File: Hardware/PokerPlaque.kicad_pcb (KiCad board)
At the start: 2 copper layers, 50 x 43 mm, 7 parts, among them J1 Conn_01x05_Pin, J2 Conn_01x04_Pin, J3 Conn_01x08_Pin, J4 Conn_01x02_Pin, U2 ATtiny1616-M

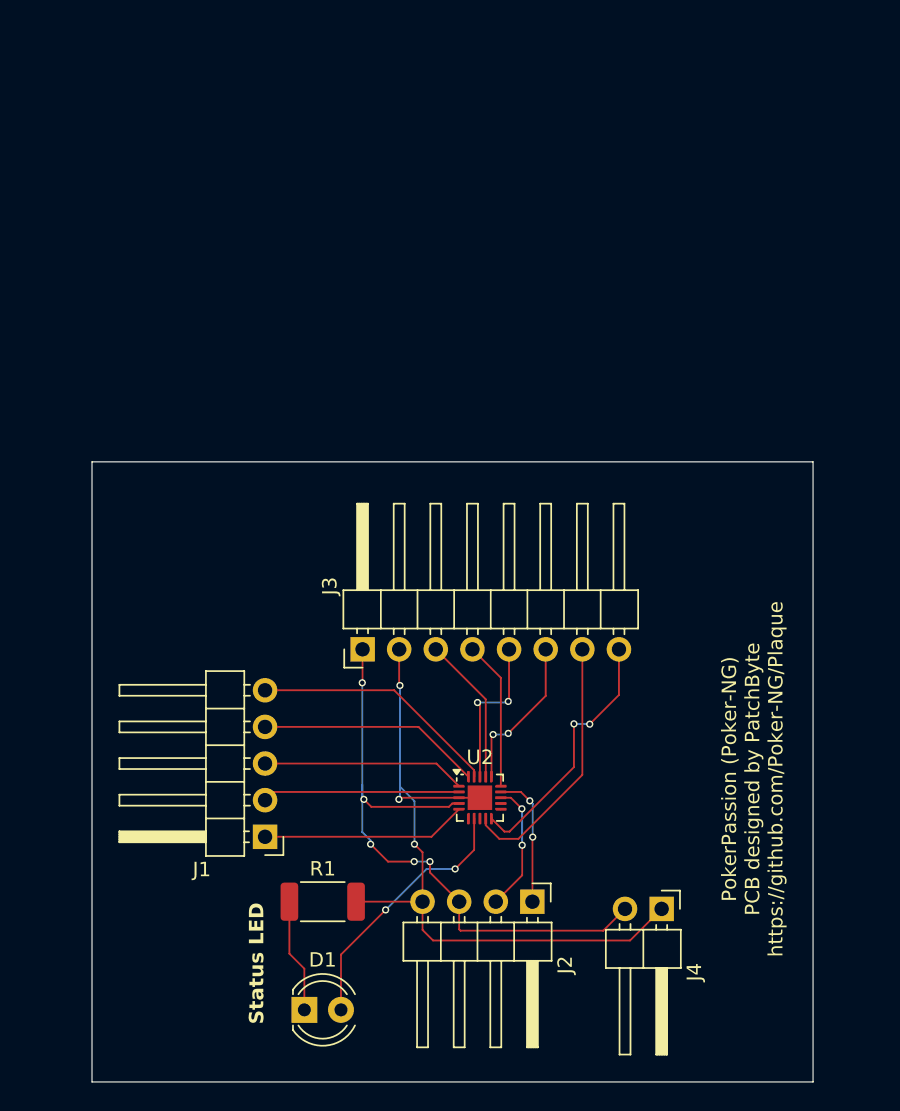
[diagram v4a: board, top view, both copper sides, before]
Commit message: feat: new riscv design
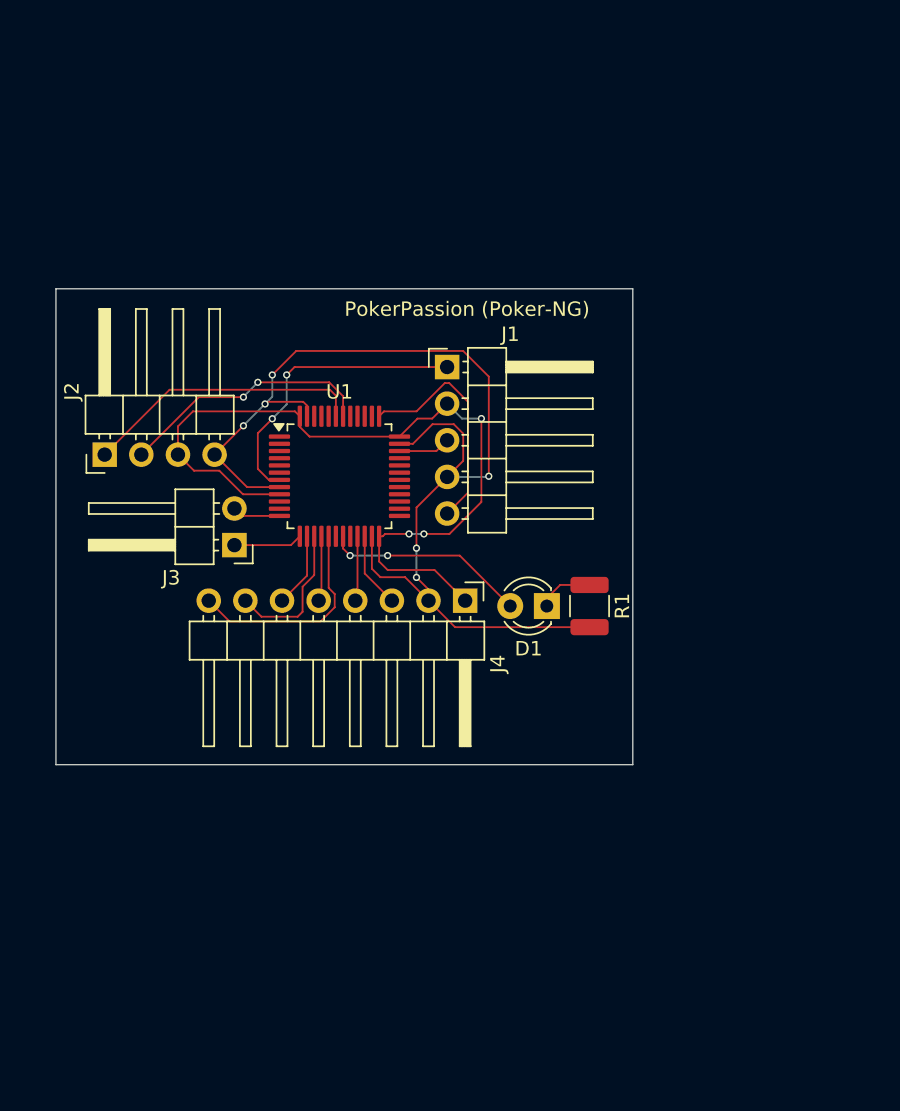
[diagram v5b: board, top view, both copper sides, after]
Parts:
- removed U2: ATtiny1616-M, Package_DFN_QFN:VQFN-20-1EP_3x3mm_P0.4mm_EP1.7x1.7mm
- added U1: CH32V203C8T6, Package_QFP:LQFP-48_7x7mm_P0.5mm, F.Cu at (43.2, 51.0)
- D1: value LED -> NFD3401URD LED; footprint LED_THT:LED_D4.0mm -> LED_THT:LED_D3.0mm
- J3: value Conn_01x08_Pin -> Conn_01x02_Pin; footprint Connector_PinHeader_2.54mm:PinHeader_1x08_P2.54mm_Horizontal -> Connector_PinHeader_2.54mm:PinHeader_1x02_P2.54mm_Horizontal
- J4: value Conn_01x02_Pin -> Conn_01x08_Pin; footprint Connector_PinHeader_2.54mm:PinHeader_1x02_P2.54mm_Horizontal -> Connector_PinHeader_2.54mm:PinHeader_1x08_P2.54mm_Horizontal
- R1: footprint Resistor_SMD:R_2010_5025Metric -> Resistor_SMD:R_1210_3225Metric
- moved J2 42.9 mm to (26.9, 49.5), turned to 90 degrees
- moved J1 34.9 mm to (50.6, 43.4), turned to 0 degrees
- moved D1 32.7 mm to (57.5, 60.0), turned to 180 degrees
- moved R1 27.6 mm to (60.5, 60.0), turned to -90 degrees
- moved J4 25.3 mm to (51.9, 59.6)
- moved J3 11.5 mm to (35.9, 55.8), turned to 180 degrees
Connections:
- D1 pad 2: Led0 -> DEBUG_LED0
- J1 pad 1: /Ss0 -> RST
- J1 pad 2: /Sck0 -> +3.3V
- J1 pad 3: /Miso0 -> SWDIO
- J1 pad 4: /Mosi0 -> GND
- J1 pad 5: /Reset0 -> SWCLK
- J2 pad 1: SCL -> I2C1_SDA
- J2 pad 2: SDA -> I2C1_SCL
- J2 pad 3: VCC -> +3.3V
- J3 pad 1: VCC -> RESERVED_UART_RX
- J3 pad 2: GND -> RESERVED_UART_TX
- J4 pad 1: GND -> +3.3V
- J4 pad 2: VCC -> GND
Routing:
- net +3.3V: track 0.00 -> 56.8 mm, vias 0 -> 3
- net VCC: track 44.0 -> 0.00 mm, vias 5 -> 0
- net GND: track 49.1 -> 80.2 mm, vias 3 -> 6
- net RST: track 0.00 -> 20.5 mm, vias 0 -> 2
- net I2C1_SDA: track 0.00 -> 19.5 mm
- net Led0: track 18.2 -> 0.00 mm, vias 2 -> 0
- net DspRst: track 18.1 -> 0.00 mm
- net DspBusy: track 18.1 -> 0.00 mm, vias 2 -> 0
- net I2C1_SCL: track 0.00 -> 17.9 mm, vias 0 -> 2
- net /Reset0: track 17.3 -> 0.00 mm
- net SWCLK: track 0.00 -> 16.0 mm
- net /Mosi0: track 15.5 -> 0.00 mm
- net DISPLAY_MOSI1: track 0.00 -> 14.8 mm
- net /Ss0: track 14.2 -> 0.00 mm
- net /Miso0: track 14.1 -> 0.00 mm
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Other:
- board size 50 x 43 mm -> 40 x 33 mm
- board text added: "PokerPassion (Poker-NG)"
- board text removed: "PokerPassion (Poker-NG) PCB designed by PatchByte https://github.com/Poker-NG/Plaque"
- board text removed: "Status LED"

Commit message: feat: added some necessities
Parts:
- added R2: 10k Ohm, Resistor_SMD:R_1210_3225Metric, F.Cu at (30.5, 29.5)
- added R3: 10k Ohm, Resistor_SMD:R_1210_3225Metric, F.Cu at (50.5, 57.5)
- added SW1: KH-6X6X6H-STM, Button_Switch_SMD:SW_Push_1P1T_NO_6x6mm_H9.5mm, F.Cu at (51.0, 26.0)
- D1: value NFD3401URD LED -> NFD3401URD
- J1: value Conn_01x05_Pin -> A2541WR-5P
- J2: value Conn_01x04_Pin -> A2541WR-4P
- J3: value Conn_01x02_Pin -> A2541WR-2P
- J4: value Conn_01x08_Pin -> A2541WR-8P
- moved J2 20.0 mm to (34.4, 31.0)
- moved J3 15.7 mm to (24.3, 45.2), turned to 90 degrees
- moved J4 12.2 mm to (45.8, 49.0)
- moved R1 11.9 mm to (50.5, 53.5), turned to 180 degrees
- moved U1 11.6 mm to (36.8, 41.3)
- moved J1 10.5 mm to (44.5, 34.9)
- moved D1 4.64 mm to (54.5, 56.5), turned to 0 degrees
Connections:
- U1 pad 1: unconnected-(U1-VBAT-Pad1) -> +3.3V
- U1 pad 20: unconnected-(U1-PB2-Pad20) -> BOOT1
- U1 pad 44: unconnected-(U1-BOOT0-Pad44) -> BOOT0
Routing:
- net +3.3V: track 56.8 -> 91.5 mm, vias 3 -> 1
- net BOOT0: track 0.00 -> 34.0 mm, vias 0 -> 2
- net BOOT1: track 0.00 -> 24.1 mm
- net DEBUG_LED0: track 14.1 -> 30.2 mm
- net I2C1_SDA: track 19.5 -> 7.05 mm
- net I2C1_SCL: track 17.9 -> 6.21 mm, vias 2 -> 0
- net RESERVED_UART_RX: track 4.79 -> 10.5 mm
- net DISPLAY_MOSI1: track 14.8 -> 10.5 mm, vias 0 -> 2
- net SWCLK: track 16.0 -> 12.2 mm
- net RST: track 20.5 -> 17.5 mm, vias 2 -> 1
- net RESERVED_UART_TX: track 3.34 -> 6.26 mm
- net GND: track 80.2 -> 82.5 mm, vias 6 -> 2
- net DISPLAY_SCK1: track 10.1 -> 8.88 mm
- net DISPLAY_SS1: track 5.18 -> 4.09 mm
- net DISPLAY_MISO1: track 4.54 -> 3.55 mm
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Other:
- board size 40 x 33 mm -> 36.5 x 40.5 mm
- board text removed: "PokerPassion (Poker-NG)"

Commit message: feat: changed some things
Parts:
- moved J3 14.3 mm to (24.2, 30.9)
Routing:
- net RESERVED_UART_RX: track 10.5 -> 21.1 mm, vias 0 -> 2
- net RESERVED_UART_TX: track 6.26 -> 16.2 mm
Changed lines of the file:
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@@
 	(footprint "Connector_PinHeader_2.54mm:PinHeader_1x02_P2.54mm_Horizontal"
 		(layer "F.Cu")
-		(at 24.255248 45.208264 90)
+		(at 24.225 30.875 90)
 		(descr "Through hole angled pin header, 1x02, 2.54mm pitch, 6mm pin length, single row")
 		(tags "Through hole angled pin header THT 1x02 2.54mm single row")
@@
 	)
 	(segment
-		(start 32.5875 44.0875)
-		(end 27.916012 44.0875)
-		(width 0.127)
+		(start 26.765 30.875)
+		(end 28.19 32.3)
+		(width 0.2)
 		(layer "F.Cu")
 		(net 10)
 	)
 	(segment
-		(start 27.916012 44.0875)
-		(end 26.795248 45.208264)
-		(width 0.127)
+		(start 31.5875 44.0875)
+		(end 32.5875 44.0875)
+		(width 0.2)
 		(layer "F.Cu")
 		(net 10)
 	)
 	(segment
-		(start 25.368748 46.321764)
-		(end 33.178236 46.321764)
-		(width 0.127)
+		(start 28.19 32.3)
+		(end 28.19 40.69)
+		(width 0.2)
+		(layer "F.Cu")
+		(net 10)
+	)
+	(segment
+		(start 28.19 40.69)
+		(end 31.5875 44.0875)
+		(width 0.2)
+		(layer "F.Cu")
+		(net 10)
+	)
+	(segment
+		(start 24.225 30.875)
+		(end 24.225 31.925)
+		(width 0.2)
 		(layer "F.Cu")
 		(net 11)
 	)
 	(segment
-		(start 33.178236 46.321764)
+		(start 31.5 45.5)
 		(end 34 45.5)
-		(width 0.127)
+		(width 0.2)
 		(layer "F.Cu")
 		(net 11)
 	)
 	(segment
-		(start 24.255248 45.208264)
-		(end 25.368748 46.321764)
-		(width 0.127)
+		(start 25.8 33.5)
+		(end 27.5 33.5)
+		(width 0.2)
 		(layer "F.Cu")
 		(net 11)
 	)
+	(segment
+		(start 24.225 31.925)
+		(end 25.8 33.5)
+		(width 0.2)
+		(layer "F.Cu")
+		(net 11)
+	)
+	(segment
+		(start 29.5 43.5)
+		(end 31.5 45.5)
+		(width 0.2)
+		(layer "F.Cu")
+		(net 11)
+	)
+	(via
+		(at 27.5 33.5)
+		(size 0.6)
+		(drill 0.3)
+		(layers "F.Cu" "B.Cu")
+		(net 11)
+	)
+	(via
+		(at 29.5 43.5)
+		(size 0.6)
+		(drill 0.3)
+		(layers "F.Cu" "B.Cu")
+		(net 11)
+	)
+	(segment
+		(start 27.5 33.5)
+		(end 29.5 35.5)
+		(width 0.2)
+		(layer "B.Cu")
+		(net 11)
+	)
+	(segment
+		(start 29.5 35.5)
+		(end 29.5 43.5)
+		(width 0.2)
+		(layer "B.Cu")
+		(net 11)
+	)

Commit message: feat: revamped
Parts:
- moved R2 28.7 mm to (55.0, 44.5), turned to 0 degrees
- moved J3 25.0 mm to (34.4, 53.8), turned to 180 degrees
- moved J1 21.5 mm to (24.9, 43.9), turned to 90 degrees
- moved R1 12.9 mm to (62.0, 59.5), turned to -90 degrees
- moved SW1 12.3 mm to (58.8, 35.5)
- moved J2 11.8 mm to (42.2, 39.9)
- moved J4 10.7 mm to (51.4, 58.1)
- moved U1 9.92 mm to (43.3, 48.8)
- moved R3 7.91 mm to (55.0, 51.0)
- moved D1 3.64 mm to (57.5, 58.5), turned to 180 degrees
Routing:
- net +3.3V: track 91.5 -> 133.1 mm, vias 1 -> 7
- net SWDIO: track 3.76 -> 23.8 mm, vias 0 -> 2
- net RESERVED_UART_RX: track 21.1 -> 6.57 mm, vias 2 -> 0
- net RESERVED_UART_TX: track 16.2 -> 4.91 mm
- net DEBUG_LED0: track 30.2 -> 20.5 mm
- net BOOT1: track 24.1 -> 16.6 mm, vias 0 -> 4
- net SWCLK: track 12.2 -> 18.5 mm
- net DISPLAY_MOSI1: track 10.5 -> 15.3 mm, vias 2 -> 0
- net BOOT0: track 34.0 -> 30.2 mm, vias 2 -> 4
- net DISPLAY_SS1: track 4.09 -> 6.21 mm
- net DISPLAY_MISO1: track 3.55 -> 5.57 mm
- net DISPLAY_RESET: track 3.57 -> 5.56 mm
- net I2C1_SDA: track 7.05 -> 5.08 mm
- net RST: track 17.5 -> 16.4 mm, vias 1 -> 0
- net DISPLAY_SCK1: track 8.88 -> 9.93 mm, vias 0 -> 2
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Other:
- board size 36.5 x 40.5 mm -> 43.1 x 40.2 mm
